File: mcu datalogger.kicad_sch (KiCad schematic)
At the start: 25 parts, among them U1 24LC1025, U2 24LC1025, U3 DS1337S_, U4 ATMEGA328P-AU, Y1 32.768KHz, Y2 16MHz

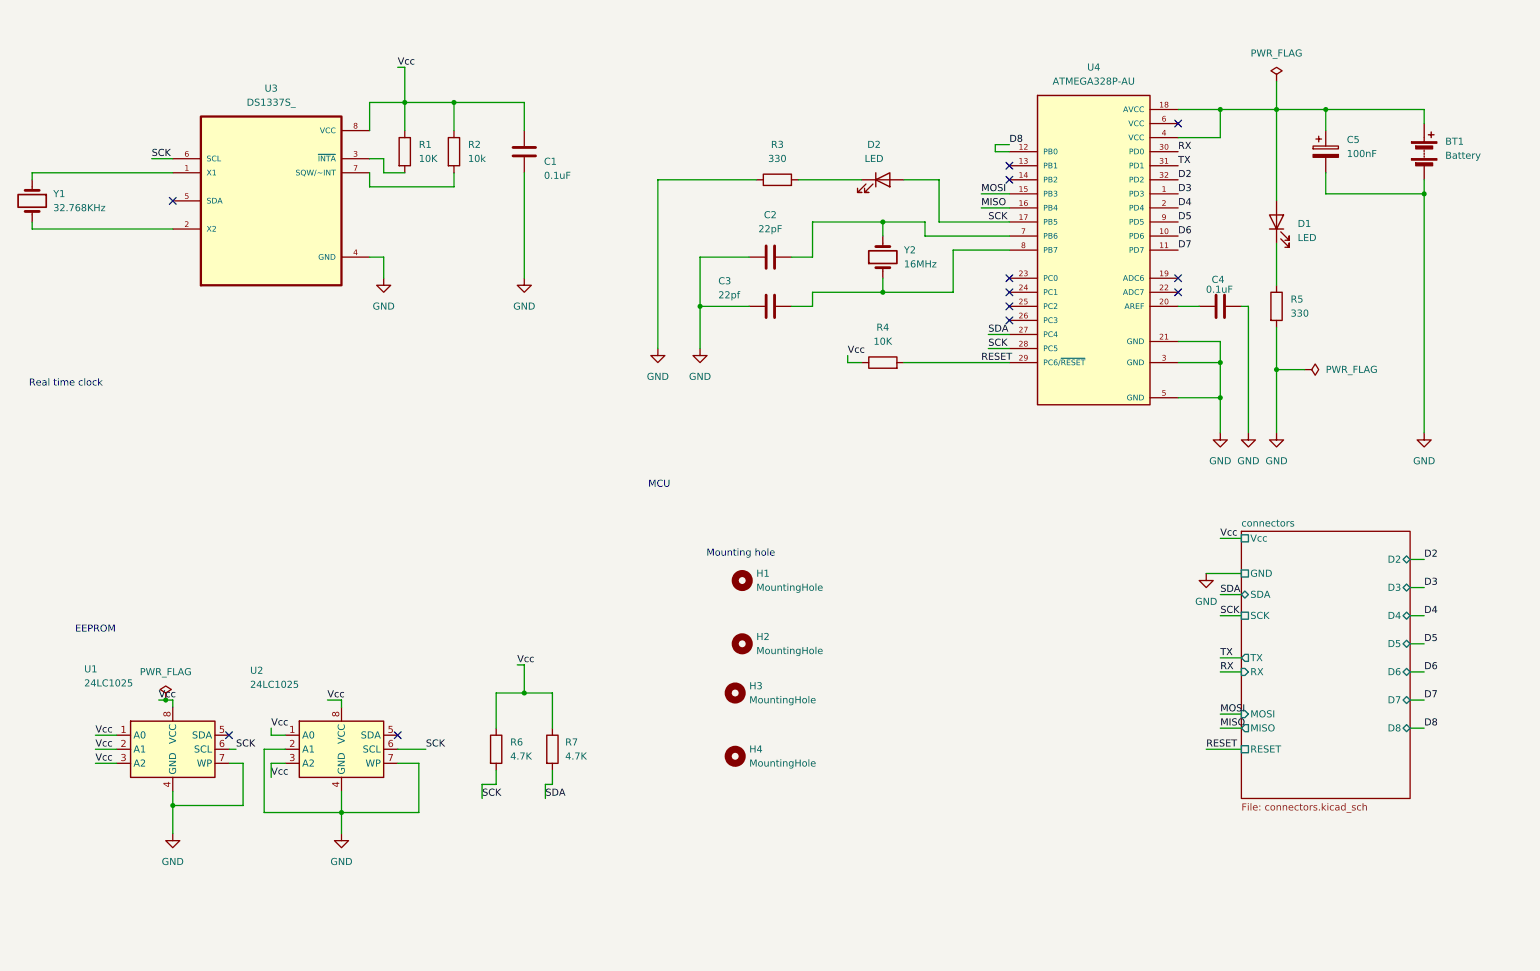
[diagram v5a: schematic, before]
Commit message: Add schematic annotations and documentation to 4-layer design
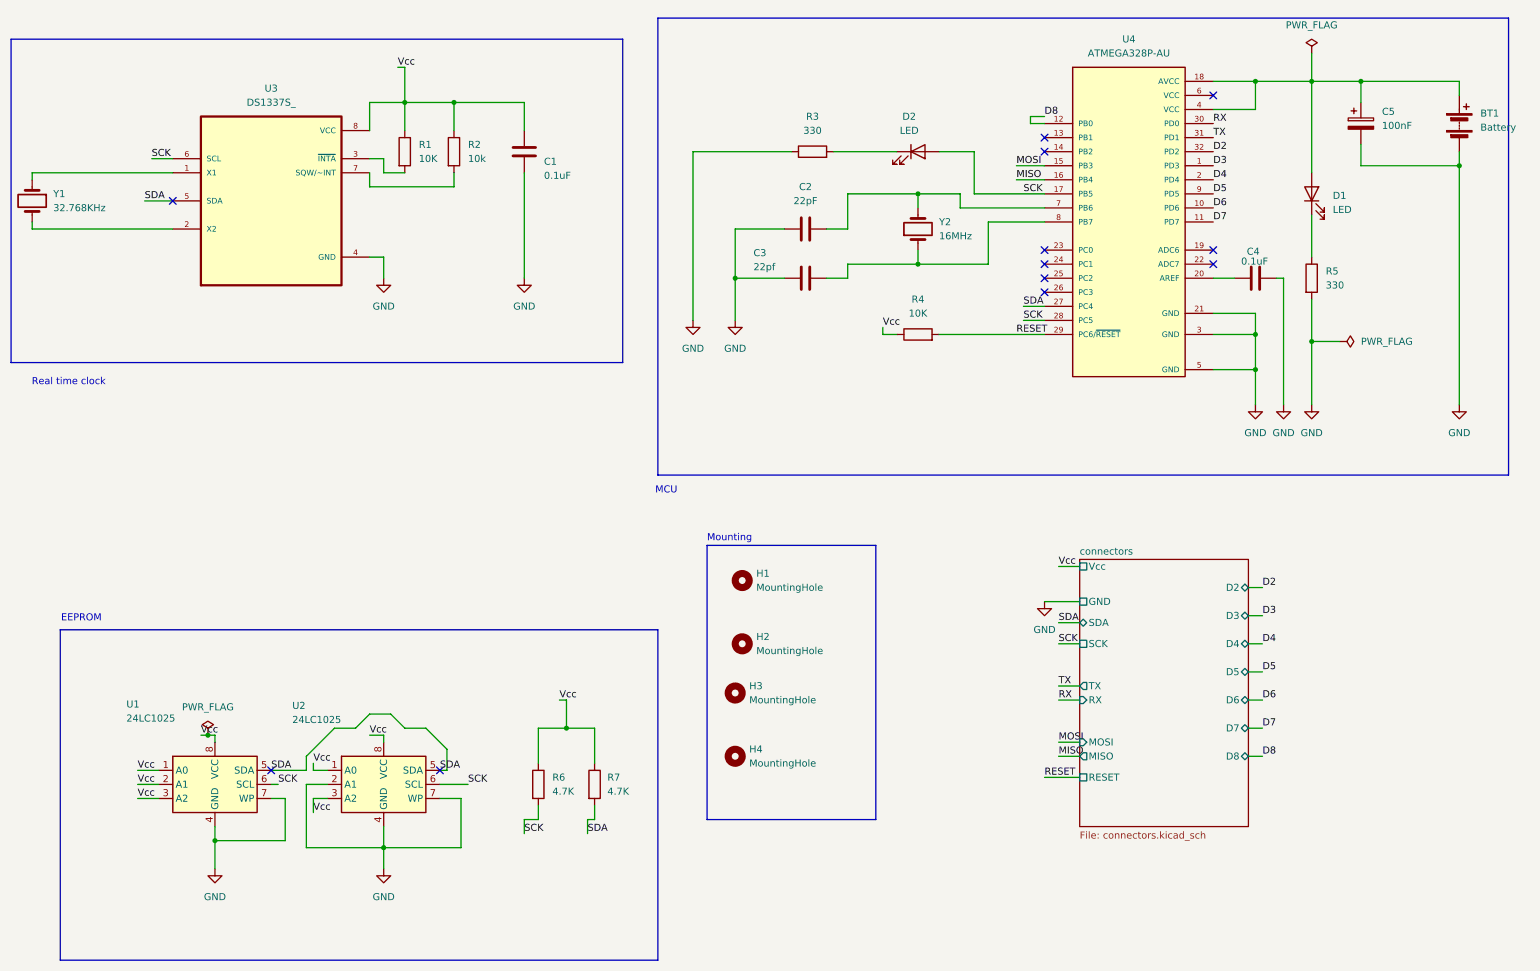
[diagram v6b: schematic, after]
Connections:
- net SDA: now also U1.5 (SDA), U2.5 (SDA), U3.5 (SDA)
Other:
- note added: "Mounting"
- note removed: "Mounting hole"
- moved on the sheet: BT1, C2, C3, C4, C5, D1, D2, R3, R4, R5, R6, R7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
